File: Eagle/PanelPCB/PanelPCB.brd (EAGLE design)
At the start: 42.9 x 81.3 mm, 8 parts, among them M1 RARNDT-MISCELANEOUS_FEATHERBO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

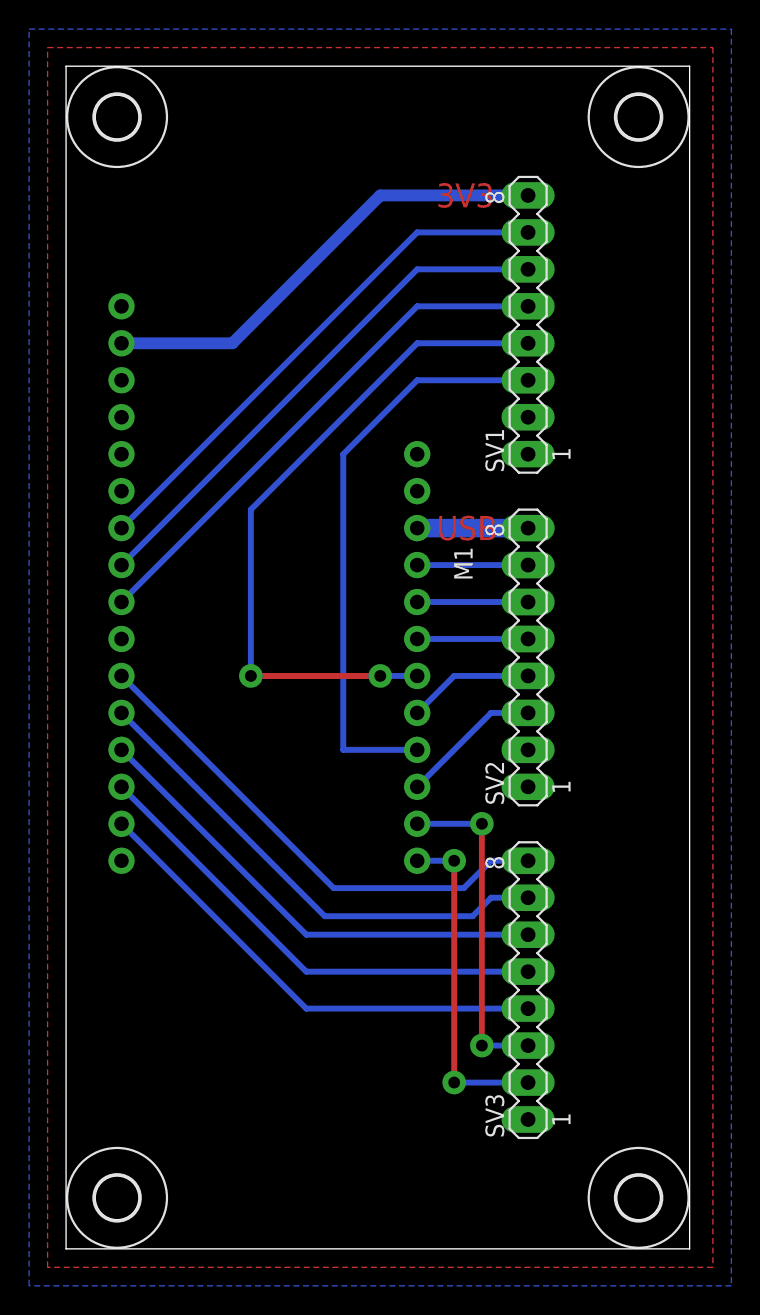
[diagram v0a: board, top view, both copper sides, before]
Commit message: Updated PCB board to allow more clearance
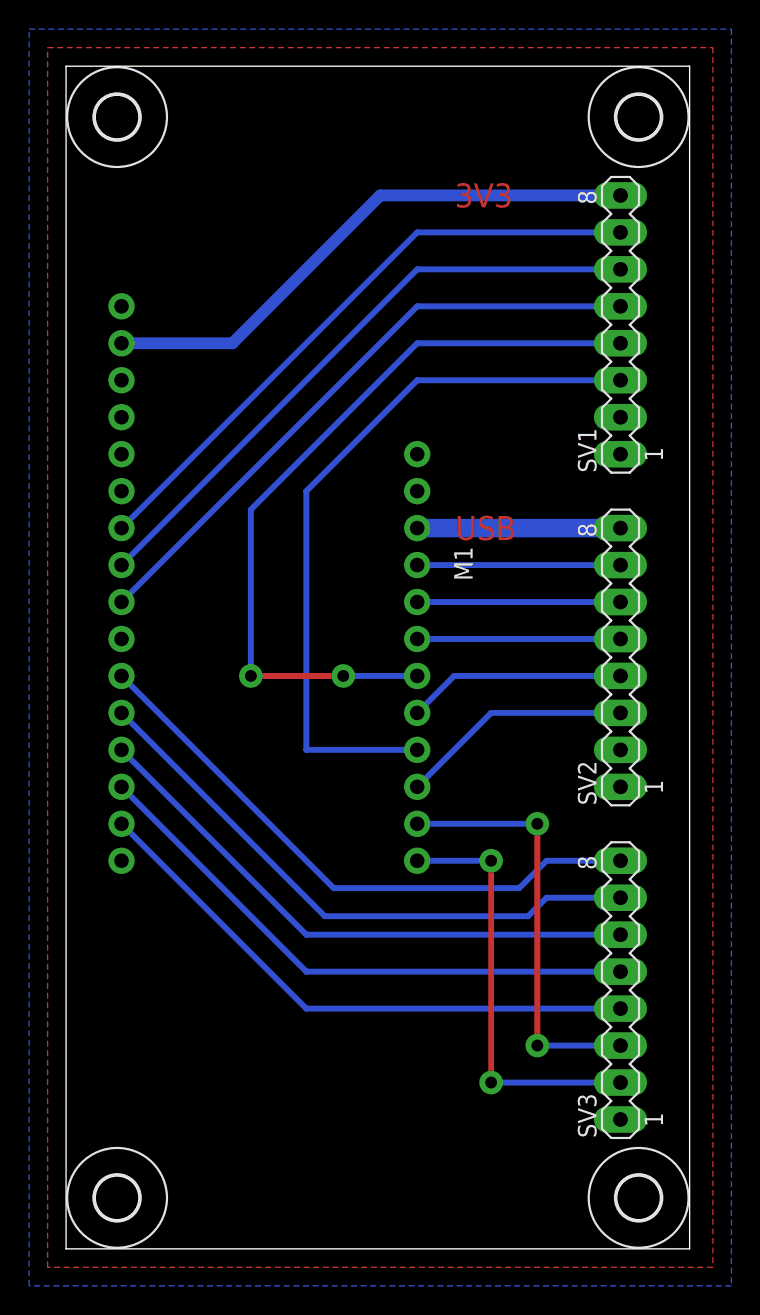
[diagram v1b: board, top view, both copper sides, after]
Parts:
- moved SV1 6.35 mm to (38.1, 57.1)
- moved SV2 6.35 mm to (38.1, 34.3)
- moved SV3 6.35 mm to (38.1, 11.4)
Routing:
- net 32: track 40.2 -> 50.1 mm
- net TX: track 33.2 -> 39.6 mm
- net RX: track 33.2 -> 39.6 mm
- net MO: track 34.3 -> 40.6 mm
- net USB: track 7.62 -> 14.0 mm
- net SDA: track 22.9 -> 29.2 mm
- net SCL: track 22.9 -> 29.2 mm
- net SCK: track 34.8 -> 41.1 mm
- net MI: track 33.2 -> 39.6 mm
- net 3V3: track 32.1 -> 38.5 mm
- net 33: track 46.6 -> 53.0 mm
- net 27: track 7.62 -> 14.0 mm
- net 15: track 8.67 -> 15.0 mm
- net 14: track 9.72 -> 16.1 mm
- net 13: track 7.62 -> 14.0 mm
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
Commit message: Updated PCB design
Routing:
- net SCL: track 29.2 -> 43.2 mm
- net SDA: track 29.2 -> 36.8 mm
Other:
- board text added: "3V3 A2 A3 A4 33 32 GND GND"
- board text added: "SCK MO MI RX TX SCL SDA GND"
- board text added: "USB 13 12 27 15 14 GND GND"
- board text removed: "3V3"
- board text removed: "USB"
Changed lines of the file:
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@@
 <layer number="19" name="Unrouted" color="6" fill="1" visible="yes" active="yes"/>
 <layer number="20" name="Dimension" color="24" fill="1" visible="yes" active="yes"/>
-<layer number="21" name="tPlace" color="7" fill="1" visible="yes" active="yes"/>
-<layer number="22" name="bPlace" color="7" fill="1" visible="yes" active="yes"/>
+<layer number="21" name="tPlace" color="7" fill="1" visible="no" active="yes"/>
+<layer number="22" name="bPlace" color="7" fill="1" visible="no" active="yes"/>
 <layer number="23" name="tOrigins" color="15" fill="1" visible="yes" active="yes"/>
 <layer number="24" name="bOrigins" color="15" fill="1" visible="yes" active="yes"/>
@@
 <wire x1="42.85" y1="74.92" x2="0" y2="74.92" width="0" layer="20"/>
 <wire x1="0" y1="74.92" x2="0" y2="-6.35" width="0" layer="20"/>
-<text x="28.702" y="66.04" size="1.651" layer="1" font="vector" ratio="25" align="center">3V3</text>
-<text x="28.829" y="43.18" size="1.651" layer="1" font="vector" ratio="25" align="center">USB</text>
-<dimension x1="42.85" y1="74.92" x2="0" y2="74.92" x3="21.425" y3="80.01" textsize="1.778" layer="1"/>
-<dimension x1="0" y1="74.92" x2="0" y2="-6.35" x3="-7.62" y3="34.285" textsize="1.778" layer="1"/>
-<dimension x1="3.5052" y1="-2.8448" x2="39.3446" y2="-2.8448" x3="21.4249" y3="-12.7" textsize="1.778" layer="1"/>
-<dimension x1="39.3446" y1="-2.8448" x2="39.3446" y2="71.4248" x3="54.61" y3="34.29" textsize="1.778" layer="1"/>
+<text x="30.607" y="57.15" size="1.524" layer="51" font="vector" ratio="15" distance="70" align="center">3V3
+A2
+A3
+A4
+33
+32
+GND
+GND</text>
+<dimension x1="42.85" y1="74.92" x2="0" y2="74.92" x3="21.425" y3="80.01" textsize="1.778" layer="20"/>
+<dimension x1="0" y1="74.92" x2="0" y2="-6.35" x3="-7.62" y3="34.285" textsize="1.778" layer="20"/>
+<dimension x1="39.3446" y1="-2.8448" x2="39.3446" y2="71.4248" x3="54.61" y3="34.29" textsize="1.778" layer="20"/>
+<text x="30.607" y="34.29" size="1.524" layer="51" font="vector" ratio="15" distance="70" align="center">USB
+13
+12
+27
+15
+14
+GND
+GND</text>
+<text x="30.607" y="11.43" size="1.524" layer="51" font="vector" ratio="15" distance="70" align="center">SCK
+MO
+MI
+RX
+TX
+SCL
+SDA
+GND</text>
+<dimension x1="3.5052" y1="-2.8448" x2="39.3446" y2="-2.8448" x3="21.4249" y3="-15.24" textsize="1.778" layer="20"/>
 </plain>
 <attributes>
@@
 </autorouter>
 <elements>
-<element name="M1" library="StewartPlatform" package="RARNDT-MISCELANEOUS_FEATHERBOARD_ESP32" value="RARNDT-MISCELANEOUS_FEATHERBOARD_ESP32FETHERWING_DIM_ESP32" x="13.97" y="39.37" smashed="yes" rot="R270">
-<attribute name="NAME" x="26.67" y="41.91" size="1.27" layer="21" rot="R270"/>
-</element>
+<element name="M1" library="StewartPlatform" package="RARNDT-MISCELANEOUS_FEATHERBOARD_ESP32" value="RARNDT-MISCELANEOUS_FEATHERBOARD_ESP32FETHERWING_DIM_ESP32" x="13.97" y="39.37" smashed="yes" rot="R270"/>
 <element name="SV1" library="con-lstb" library_urn="urn:adsk.eagle:library:162" package="MA08-1" package3d_urn="urn:adsk.eagle:package:8343/1" value="" x="38.1" y="57.15" smashed="yes" rot="R90">
 <attribute name="MF" value="" x="38.1" y="57.15" size="1.778" layer="27" rot="R90" display="off"/>
 <attribute name="MPN" value="" x="38.1" y="57.15" size="1.778" layer="27" rot="R90" display="off"/>
-<attribute name="NAME" x="36.449" y="46.99" size="1.27" layer="25" ratio="10" rot="R90"/>
 <attribute name="OC_FARNELL" value="unknown" x="38.1" y="57.15" size="1.778" layer="27" rot="R90" display="off"/>
 <attribute name="OC_NEWARK" value="unknown" x="38.1" y="57.15" size="1.778" layer="27" rot="R90" display="off"/>
@@
 <attribute name="MF" value="" x="38.1" y="34.29" size="1.778" layer="27" rot="R90" display="off"/>
 <attribute name="MPN" value="" x="38.1" y="34.29" size="1.778" layer="27" rot="R90" display="off"/>
-<attribute name="NAME" x="36.449" y="24.13" size="1.27" layer="25" ratio="10" rot="R90"/>
 <attribute name="OC_FARNELL" value="unknown" x="38.1" y="34.29" size="1.778" layer="27" rot="R90" display="off"/>
 <attribute name="OC_NEWARK" value="unknown" x="38.1" y="34.29" size="1.778" layer="27" rot="R90" display="off"/>
@@
 <attribute name="MF" value="" x="38.1" y="11.43" size="1.778" layer="27" rot="R90" display="off"/>
 <attribute name="MPN" value="" x="38.1" y="11.43" size="1.778" layer="27" rot="R90" display="off"/>
-<attribute name="NAME" x="36.449" y="1.27" size="1.27" layer="25" ratio="10" rot="R90"/>
 <attribute name="OC_FARNELL" value="unknown" x="38.1" y="11.43" size="1.778" layer="27" rot="R90" display="off"/>
 <attribute name="OC_NEWARK" value="unknown" x="38.1" y="11.43" size="1.778" layer="27" rot="R90" display="off"/>
@@
 <contactref element="M1" pad="11"/>
 <contactref element="SV3" pad="8"/>
-<wire x1="38.1" y1="20.32" x2="33.02" y2="20.32" width="0.4064" layer="16"/>
-<wire x1="33.02" y1="20.32" x2="31.1404" y2="18.4404" width="0.4064" layer="16"/>
+<wire x1="38.1" y1="20.32" x2="31.75" y2="20.32" width="0.4064" layer="16"/>
+<wire x1="31.75" y1="20.32" x2="29.8704" y2="18.4404" width="0.4064" layer="16"/>
 <wire x1="18.3896" y1="18.4404" x2="3.81" y2="33.02" width="0.4064" layer="16"/>
-<wire x1="31.1404" y1="18.4404" x2="18.3896" y2="18.4404" width="0.4064" layer="16"/>
+<wire x1="29.8704" y1="18.4404" x2="18.3896" y2="18.4404" width="0.4064" layer="16"/>
 </signal>
 <signal name="MO">
@@
 <contactref element="SV3" pad="7"/>
 <wire x1="17.78" y1="16.51" x2="3.81" y2="30.48" width="0.4064" layer="16"/>
-<wire x1="38.1" y1="17.78" x2="33.02" y2="17.78" width="0.4064" layer="16"/>
-<wire x1="33.02" y1="17.78" x2="31.75" y2="16.51" width="0.4064" layer="16"/>
-<wire x1="31.75" y1="16.51" x2="17.78" y2="16.51" width="0.4064" layer="16"/>
+<wire x1="38.1" y1="17.78" x2="31.75" y2="17.78" width="0.4064" layer="16"/>
+<wire x1="31.75" y1="17.78" x2="30.48" y2="16.51" width="0.4064" layer="16"/>
+<wire x1="30.48" y1="16.51" x2="17.78" y2="16.51" width="0.4064" layer="16"/>
 </signal>
 <signal name="MI">
@@
 <contactref element="M1" pad="18"/>
 <contactref element="SV3" pad="3"/>
-<wire x1="24.13" y1="22.86" x2="32.385" y2="22.86" width="0.4064" layer="16"/>
-<via x="32.385" y="22.86" extent="1-16" drill="0.8128"/>
-<wire x1="32.385" y1="22.86" x2="32.385" y2="7.62" width="0.4064" layer="1"/>
-<via x="32.385" y="7.62" extent="1-16" drill="0.8128"/>
-<wire x1="32.385" y1="7.62" x2="38.1" y2="7.62" width="0.4064" layer="16"/>
-<wire x1="32.385" y1="7.62" x2="38.1" y2="7.62" width="0" layer="19"/>
-<wire x1="24.13" y1="22.86" x2="32.385" y2="22.86" width="0" layer="19"/>
-<wire x1="32.385" y1="7.62" x2="38.1" y2="7.62" width="0" layer="19"/>
-<wire x1="32.385" y1="7.62" x2="38.1" y2="7.62" width="0" layer="19"/>
-<wire x1="24.13" y1="22.86" x2="32.385" y2="22.86" width="0" layer="19"/>
-<wire x1="32.385" y1="7.62" x2="38.1" y2="7.62" width="0" layer="19"/>
+<via x="17.145" y="22.86" extent="1-16" drill="0.8128"/>
+<wire x1="17.145" y1="22.86" x2="17.145" y2="7.62" width="0.4064" layer="1"/>
+<via x="17.145" y="7.62" extent="1-16" drill="0.8128"/>
+<wire x1="17.145" y1="7.62" x2="38.1" y2="7.62" width="0.4064" layer="16"/>
+<wire x1="24.13" y1="22.86" x2="17.145" y2="22.86" width="0.4064" layer="16"/>
 </signal>
 <signal name="SDA">
 <contactref element="M1" pad="17"/>
 <contactref element="SV3" pad="2"/>
-<wire x1="24.13" y1="20.32" x2="29.21" y2="20.32" width="0.4064" layer="16"/>
-<via x="29.21" y="20.32" extent="1-16" drill="0.8128"/>
-<wire x1="29.21" y1="20.32" x2="29.21" y2="5.08" width="0.4064" layer="1"/>
-<via x="29.21" y="5.08" extent="1-16" drill="0.8128"/>
-<wire x1="29.21" y1="5.08" x2="38.1" y2="5.08" width="0.4064" layer="16"/>
-<wire x1="29.21" y1="5.08" x2="38.1" y2="5.08" width="0" layer="19"/>
-<wire x1="24.13" y1="20.32" x2="29.21" y2="20.32" width="0" layer="19"/>
-<wire x1="29.21" y1="5.08" x2="38.1" y2="5.08" width="0" layer="19"/>
-<wire x1="24.13" y1="20.32" x2="29.21" y2="20.32" width="0" layer="19"/>
-<wire x1="29.21" y1="5.08" x2="38.1" y2="5.08" width="0" layer="19"/>
+<via x="20.32" y="20.32" extent="1-16" drill="0.8128"/>
+<wire x1="20.32" y1="20.32" x2="20.32" y2="5.08" width="0.4064" layer="1"/>
+<via x="20.32" y="5.08" extent="1-16" drill="0.8128"/>
+<wire x1="20.32" y1="5.08" x2="38.1" y2="5.08" width="0.4064" layer="16"/>
+<wire x1="20.32" y1="20.32" x2="24.13" y2="20.32" width="0.4064" layer="16"/>
 </signal>
 </signals>
@@
 </drawing>
 <compatibility>
+<note version="6.3" minversion="6.2.2" severity="warning">
+Since Version 6.2.2 text objects can contain more than one line,
+which will not be processed correctly with this version.
+</note>
 <note version="8.2" severity="warning">
 Since Version 8.2, EAGLE supports online libraries. The ids

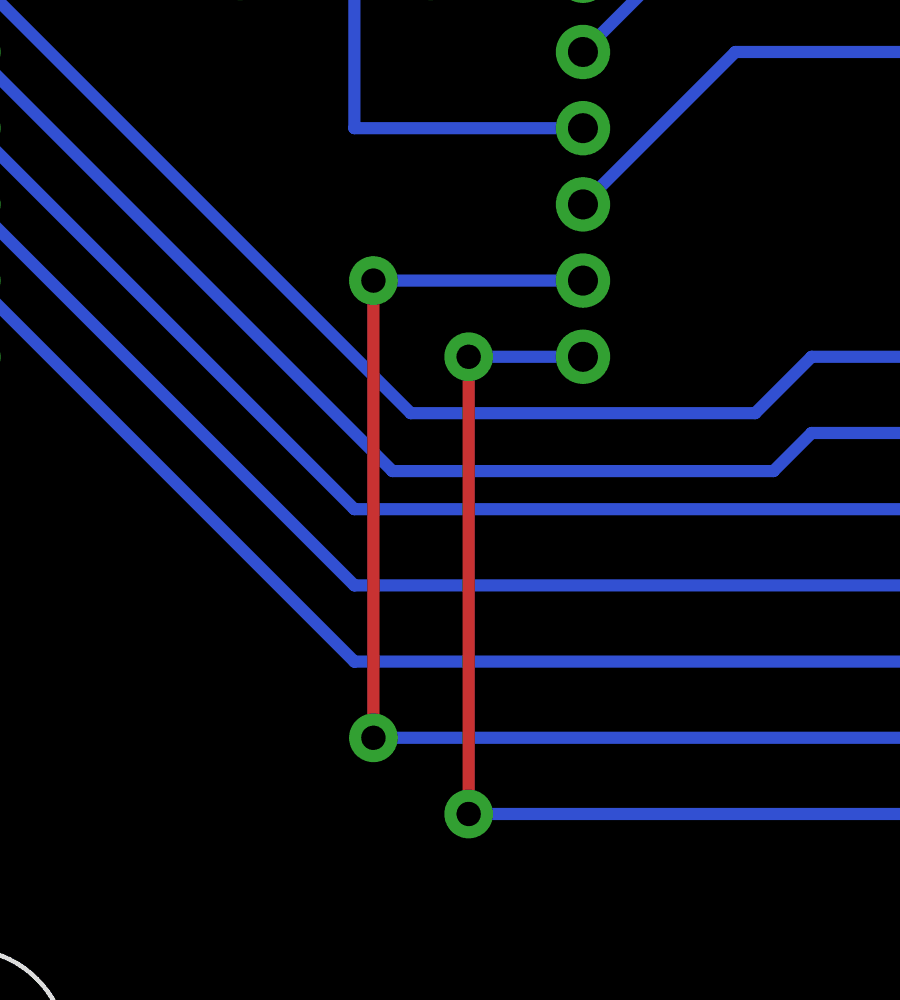
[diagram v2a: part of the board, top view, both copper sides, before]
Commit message: Updated DrawingBoard eagle files for cutting/printing
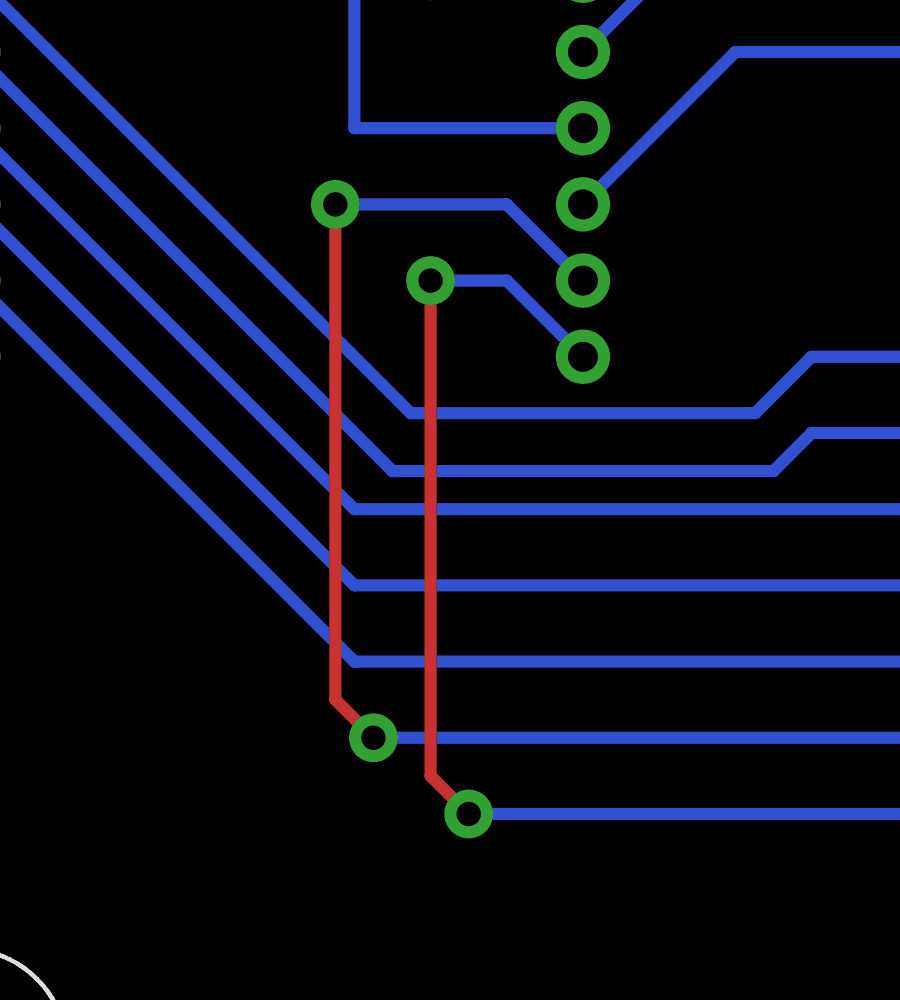
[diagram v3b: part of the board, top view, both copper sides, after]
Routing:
- net SDA: track 36.8 -> 42.2 mm
- net SCL: track 43.2 -> 48.6 mm
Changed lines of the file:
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@@
 <contactref element="M1" pad="18"/>
 <contactref element="SV3" pad="3"/>
-<via x="17.145" y="22.86" extent="1-16" drill="0.8128"/>
-<wire x1="17.145" y1="22.86" x2="17.145" y2="7.62" width="0.4064" layer="1"/>
+<via x="15.875" y="25.4" extent="1-16" drill="0.8128"/>
+<wire x1="15.875" y1="25.4" x2="15.875" y2="8.89" width="0.4064" layer="1"/>
+<wire x1="15.875" y1="8.89" x2="17.145" y2="7.62" width="0.4064" layer="1"/>
 <via x="17.145" y="7.62" extent="1-16" drill="0.8128"/>
 <wire x1="17.145" y1="7.62" x2="38.1" y2="7.62" width="0.4064" layer="16"/>
-<wire x1="24.13" y1="22.86" x2="17.145" y2="22.86" width="0.4064" layer="16"/>
+<wire x1="24.13" y1="22.86" x2="21.59" y2="25.4" width="0.4064" layer="16"/>
+<wire x1="21.59" y1="25.4" x2="15.875" y2="25.4" width="0.4064" layer="16"/>
 </signal>
 <signal name="SDA">
 <contactref element="M1" pad="17"/>
 <contactref element="SV3" pad="2"/>
-<via x="20.32" y="20.32" extent="1-16" drill="0.8128"/>
-<wire x1="20.32" y1="20.32" x2="20.32" y2="5.08" width="0.4064" layer="1"/>
+<via x="19.05" y="22.86" extent="1-16" drill="0.8128"/>
+<wire x1="19.05" y1="22.86" x2="19.05" y2="6.35" width="0.4064" layer="1"/>
+<wire x1="19.05" y1="6.35" x2="20.32" y2="5.08" width="0.4064" layer="1"/>
 <via x="20.32" y="5.08" extent="1-16" drill="0.8128"/>
 <wire x1="20.32" y1="5.08" x2="38.1" y2="5.08" width="0.4064" layer="16"/>
-<wire x1="20.32" y1="20.32" x2="24.13" y2="20.32" width="0.4064" layer="16"/>
+<wire x1="21.59" y1="22.86" x2="24.13" y2="20.32" width="0.4064" layer="16"/>
+<wire x1="21.59" y1="22.86" x2="19.05" y2="22.86" width="0.4064" layer="16"/>
 </signal>
 </signals>
